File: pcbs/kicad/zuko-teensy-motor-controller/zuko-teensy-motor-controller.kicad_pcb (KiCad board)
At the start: 2 copper layers, 100 x 45 mm, 63 parts, among them J1 Conn_01x03, J10 Conn_01x03, J11 Conn_01x03, J12 Conn_01x03, J13 Conn_01x03, J14 Conn_01x02, J15 Conn_01x02, J16 Conn_01x02, J17 Conn_01x03, J18 Conn_01x03, J19 Conn_01x02, J2 Conn_01x03, J20 Conn_01x02, J21 Conn_01x02, J22 Conn_01x03, J23 Conn_01x03, J24 Conn_01x04, J25 Conn_01x03, J26 Conn_01x03, J27 Conn_01x04, J28 Conn_01x04, J29 Conn_01x04, J3 Conn_01x03, J30 Conn_01x04, J31 Conn_01x04, J32 Conn_01x04, J33 Conn_01x04, J4 Conn_01x02, J5 Conn_01x03, J6 Conn_01x03, J7 Conn_01x03, J8 Conn_01x03, J9 Conn_01x03, Q1 BSS138, Q2 BSS138, U1 ACS712xLCTR-20A, U2 Teensy4.0, U3 ULN2003

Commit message: pcb update
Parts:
- removed J23: Conn_01x03, Connector_PinHeader_2.54mm:PinHeader_1x03_P2.54mm_Vertical
- moved U3 40.5 mm to (143.5, 70.5)
- moved R14 23.5 mm to (109.9, 72.6), turned to 90 degrees
- moved R12 21.4 mm to (120.7, 72.7), turned to 90 degrees
- moved Q2 15.6 mm to (113.3, 72.6)
- moved Q1 15.6 mm to (117.2, 72.6)
- moved R7 14.3 mm to (161.3, 78.5), turned to 90 degrees
- moved R8 12.9 mm to (158.5, 78.5), turned to -90 degrees
- moved R11 11.6 mm to (117.5, 78.4)
- moved R10 11.1 mm to (143.2, 82.7)
- moved R9 11.0 mm to (143.2, 79.6)
- moved R13 9.47 mm to (111.4, 78.4)
- moved J30 7.23 mm to (153.5, 74.9)
- moved J28 6.60 mm to (149.9, 74.9)
- moved C5 6.50 mm to (86.9, 79.0)
- moved J27 6.47 mm to (153.2, 61.0)
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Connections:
- J17 pad 1: Net-(J17-Pad1) -> AUX_M1
- J17 pad 2: AUX_M1 -> Net-(J18-Pad2)
- J18 pad 1: Net-(J17-Pad1) -> AUX_M2
- J18 pad 2: AUX_M2 -> Net-(J18-Pad2)
- J22 pad 1: Net-(J17-Pad1) -> AUX_M3
- J22 pad 2: AUX_M3 -> Net-(J18-Pad2)
- JP1 pad 2: Net-(J17-Pad1) -> Net-(J18-Pad2)
- U2 pad 14: unconnected-(U2-Pad14) -> AUX_M1
- U2 pad 21: unconnected-(U2-Pad21) -> OUT4
- U2 pad 22: unconnected-(U2-Pad22) -> OUT3
- U2 pad 23: unconnected-(U2-Pad23) -> OUT2
- U2 pad 24: unconnected-(U2-Pad24) -> OUT1
- U2 pad 29: unconnected-(U2-Pad29) -> CSENSE
- U2 pad 30: unconnected-(U2-Pad30) -> VSENSE
- U2 pad 35: unconnected-(U2-Pad35) -> SDL1
- U2 pad 36: unconnected-(U2-Pad36) -> SDA1
- U2 pad 37: unconnected-(U2-Pad37) -> NEO2
- U2 pad 38: unconnected-(U2-Pad38) -> NEO1
- U2 pad 39: unconnected-(U2-Pad39) -> SW1
- U2 pad 40: unconnected-(U2-Pad40) -> AUX_M3
- U2 pad 41: unconnected-(U2-Pad41) -> SW3
- U2 pad 42: unconnected-(U2-Pad42) -> SW2
- U2 pad 43: unconnected-(U2-Pad43) -> SW4
- U2 pad 44: unconnected-(U2-Pad44) -> AUX_M2
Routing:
- net GND: track 0.00 -> 229.4 mm
- net +BATT: track 0.00 -> 127.3 mm
- net +3V3: track 0.00 -> 80.6 mm, vias 0 -> 1
- net +5V: track 0.00 -> 74.4 mm, vias 0 -> 3
- net SCL0: track 0.00 -> 28.8 mm
- net M2: track 0.00 -> 25.3 mm
- net SDA0: track 0.00 -> 25.2 mm, vias 0 -> 2
- net M1: track 0.00 -> 24.4 mm
- net CSENSE: track 0.00 -> 24.3 mm
- net M3: track 0.00 -> 24.3 mm
- net Net-(J33-Pad2): track 0.00 -> 21.0 mm
- net VSENSE: track 0.00 -> 19.5 mm
- net Net-(J33-Pad3): track 0.00 -> 17.1 mm
- net M12: track 0.00 -> 14.4 mm
- net M11: track 0.00 -> 14.1 mm
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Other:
- board size 100 x 45 mm -> 100 x 40 mm

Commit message: pcb update
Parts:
- removed the REF** at (171.4, 54.6)
- removed the REF** at (171.4, 94.0)
- removed the REF** at (77.3, 59.3)
- removed the REF** at (77.2, 93.9)
- added J23: Conn_01x02, Connector_PinHeader_2.54mm:PinHeader_1x02_P2.54mm_Vertical, F.Cu at (132.7, 64.2)
- added REF**: MountingHole_2.5mm_Pad_TopOnly, MountingHole:MountingHole_2.5mm_Pad_TopOnly, F.Cu at (197.3, 62.8)
- added REF**: MountingHole_2.5mm_Pad_TopOnly, MountingHole:MountingHole_2.5mm_Pad_TopOnly, F.Cu at (197.3, 97.2)
- added REF**: MountingHole_2.5mm_Pad_TopOnly, MountingHole:MountingHole_2.5mm_Pad_TopOnly, F.Cu at (102.8, 97.2)
- added REF**: MountingHole_2.5mm_Pad_TopOnly, MountingHole:MountingHole_2.5mm_Pad_TopOnly, F.Cu at (102.8, 62.8)
- J4: footprint Connector_AMASS:AMASS_XT60-F_1x02_P7.20mm_Vertical -> Connector_AMASS:AMASS_XT60-M_1x02_P7.20mm_Vertical
- moved R10 55.1 mm to (197.4, 72.4), turned to -90 degrees
- moved R9 52.3 mm to (195.0, 72.4), turned to -90 degrees
- moved J28 39.1 mm to (188.4, 81.7), turned to 90 degrees
- moved J30 35.1 mm to (188.4, 79.0), turned to 90 degrees
- moved U3 30.8 mm to (174.1, 66.9)
- moved J27 30.4 mm to (183.3, 64.5)
- moved J29 29.4 mm to (186.1, 64.5)
- moved J31 28.4 mm to (188.9, 64.5)
- moved J32 27.4 mm to (191.7, 64.5)
- moved J14 26.9 mm to (136.8, 64.2)
- moved J19 26.9 mm to (139.6, 64.2)
- moved J16 26.9 mm to (142.4, 64.2)
- moved C6 26.0 mm to (114.5, 74.0)
- moved R13 25.8 mm to (137.0, 81.9)
- moved C1 25.8 mm to (177.1, 93.2)
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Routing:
- net GND: track 229.4 -> 360.9 mm, vias 0 -> 8
- net +3V3: track 80.6 -> 137.4 mm, vias 1 -> 2
- net SDA1: track 0.00 -> 50.0 mm
- net SDL1: track 0.00 -> 49.8 mm
- net +5V: track 74.4 -> 123.6 mm
- net AUX_M3: track 0.00 -> 47.2 mm
- net SW4: track 0.00 -> 41.3 mm, vias 0 -> 1
- net SW3: track 0.00 -> 37.5 mm, vias 0 -> 1
- net SW2: track 0.00 -> 37.0 mm, vias 0 -> 1
- net AUX_M2: track 0.17 -> 37.0 mm, vias 0 -> 1
- net SW1: track 0.00 -> 31.4 mm, vias 0 -> 1
- net NEO1: track 0.00 -> 30.2 mm, vias 0 -> 2
- net AUX_M1: track 0.00 -> 25.7 mm, vias 0 -> 1
- net OUT1: track 0.00 -> 22.7 mm
- net OUT2: track 0.00 -> 19.7 mm
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- added copper zone on F.Cu, net GND
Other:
- board text added: "+"
- board text added: "+3"
- board text added: "+5"
- board text added: "+5V"
- board text added: "+BATT"
- board text added: "-"
- board text added: "CONTACT"
- board text added: "IMU"
- board text added: "RPi"
- board text added: "Rx"
- board text added: "SCL"
- board text added: "SDA"
- board text added: "Tx"
- board text added: "ZUKO - A ROBOT DOG! MOTOR+ CTRL - 2022 - V2"

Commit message: pcb update
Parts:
- moved R10 0.97 mm to (197.5, 71.5)
- moved R9 0.97 mm to (195.0, 71.5)
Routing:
- net GND: track 360.9 -> 522.3 mm
- net +BATT: track 129.3 -> 214.1 mm, vias 0 -> 1
- net Net-(J4-Pad1): track 12.0 -> 27.9 mm, vias 0 -> 1
- net SDA1: track 50.0 -> 51.0 mm
- net SDL1: track 49.8 -> 50.8 mm
- added copper zone on B.Cu, net GND
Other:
- board text added: "+AUX"
- board text added: "A1"
- board text added: "A2"
- board text added: "A3"
- board text added: "AUX"
- board text added: "C"
- board text added: "GND"
- board text added: "I2C AUX."
- board text added: "LED"
- board text added: "M1"
- board text added: "M10"
- board text added: "M11"
- board text added: "M12"
- board text added: "M2"
- board text added: "M3"
- board text added: "M4"
- board text added: "M5"
- board text added: "M6"
- board text added: "M7"
- board text added: "M8"
- board text added: "M9"
- board text added: "NEO1"
- board text added: "NEO2"
- board text added: "SIG."
- board text added: "SW"

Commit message: pcb update
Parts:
- moved R10 42.8 mm to (159.3, 52.1)
- moved R9 42.8 mm to (156.9, 52.1)
- moved REF** 42.6 mm to (64.9, 43.4)
- moved C3 42.6 mm to (120.1, 73.8)
- moved J17 42.6 mm to (148.5, 71.4)
- moved J18 42.6 mm to (151.1, 71.4)
- moved J21 42.6 mm to (92.1, 44.8)
- moved J22 42.6 mm to (153.8, 71.4)
- moved J25 42.6 mm to (139.1, 59.6)
- moved J29 42.6 mm to (148.2, 45.1)
- moved J30 42.6 mm to (150.5, 59.6)
- moved J32 42.6 mm to (153.8, 45.1)
- moved J5 42.6 mm to (91.3, 71.4)
- moved JP1 42.6 mm to (145.8, 67.7)
- moved R12 42.6 mm to (108.3, 56.8)
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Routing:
- net GND: track 522.3 -> 529.9 mm, vias 8 -> 46
- net M1: track 24.4 -> 25.3 mm
- net M4: track 12.4 -> 13.2 mm
- net Net-(J29-Pad2): track 12.4 -> 11.7 mm
- net OUT3: track 16.6 -> 16.1 mm
- net Net-(J31-Pad2): track 13.2 -> 12.7 mm
- net +BATT: track 214.1 -> 214.0 mm, vias 1 -> 18
- net Net-(J4-Pad1): vias 1 -> 4
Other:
- board text added: "3V3"
- board text removed: "+3"

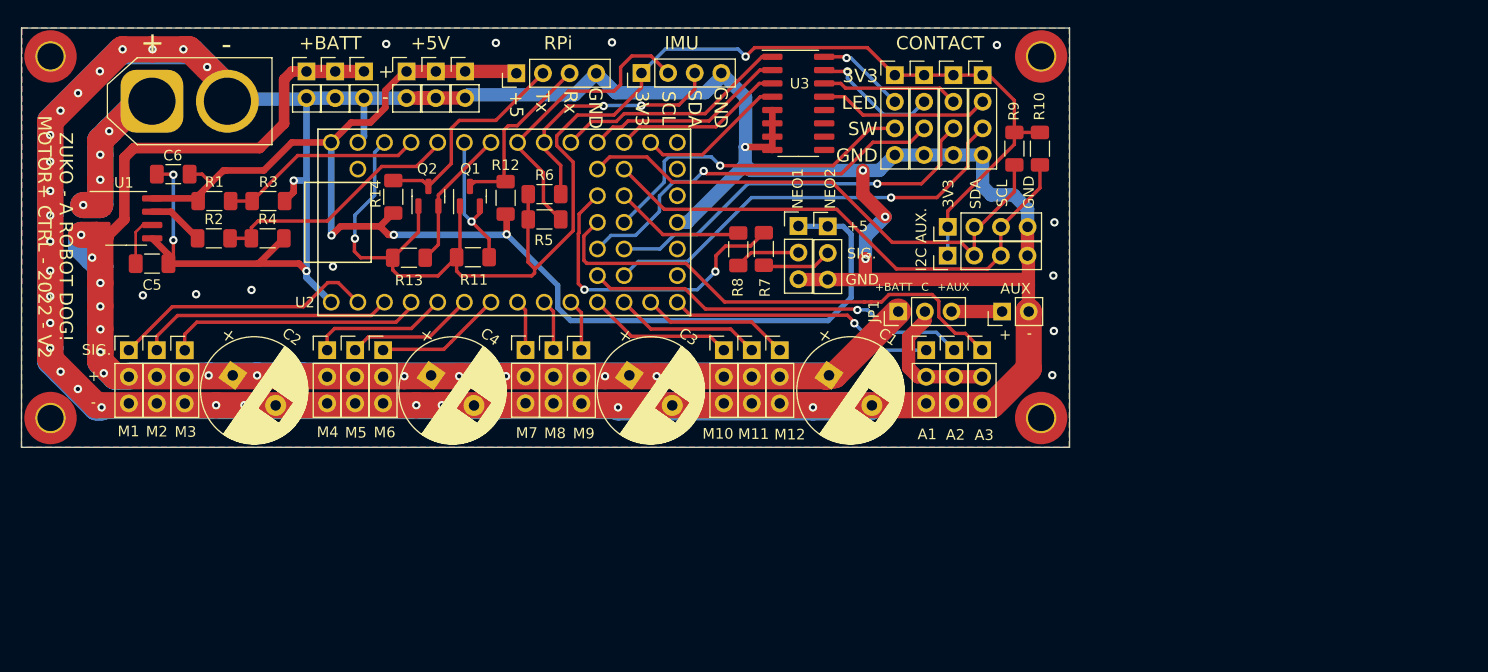
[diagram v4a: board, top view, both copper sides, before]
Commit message: pcb update - 2 layers to 4 layers
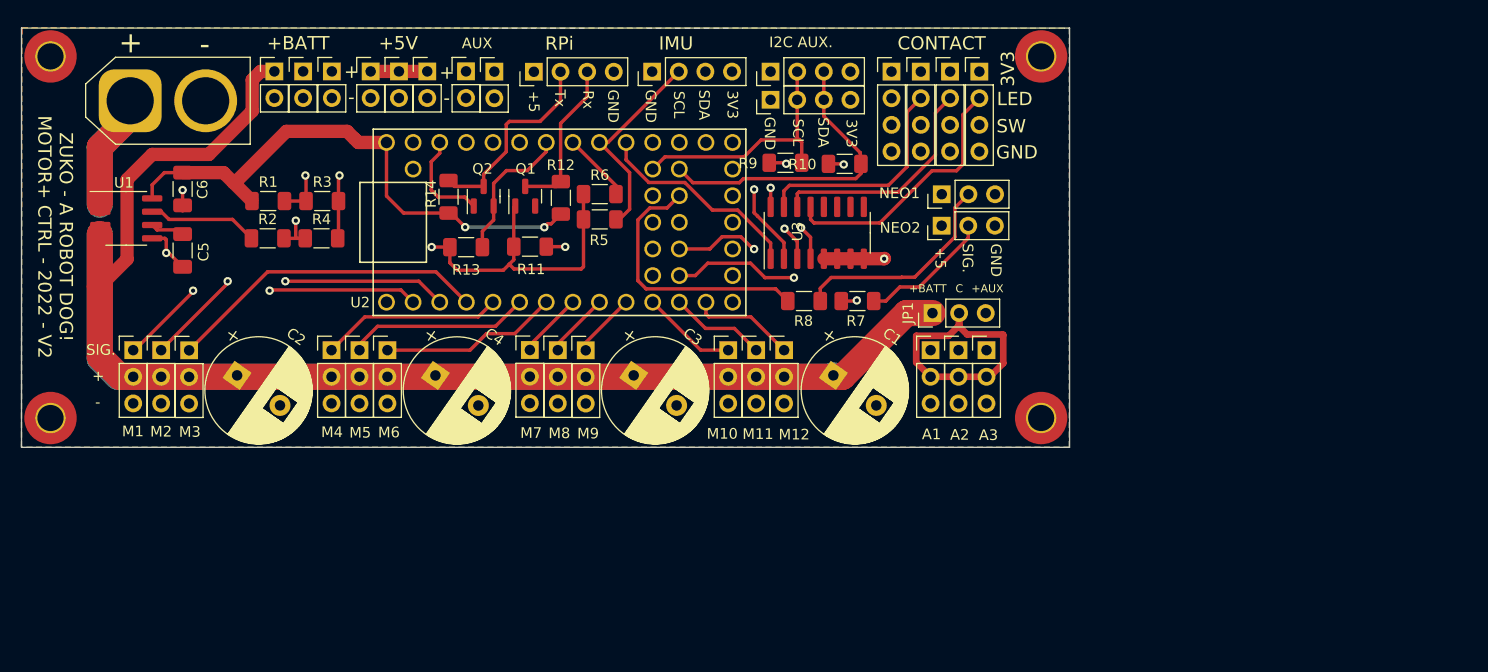
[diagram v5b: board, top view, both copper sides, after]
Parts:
- added J34: Conn_01x02, Connector_PinHeader_2.54mm:PinHeader_1x02_P2.54mm_Vertical, F.Cu at (107.2, 44.8)
- moved J20 56.0 mm to (104.5, 44.8), turned to 0 degrees
- moved J28 22.5 mm to (133.6, 47.5)
- moved J30 22.5 mm to (133.6, 44.8)
- moved R9 21.9 mm to (135.0, 53.5), turned to 0 degrees
- moved R10 18.7 mm to (140.7, 53.6), turned to 0 degrees
- moved J26 14.0 mm to (149.9, 56.5), turned to 90 degrees
- moved U3 12.5 mm to (138.1, 60.2), turned to 90 degrees
- moved J25 10.9 mm to (149.9, 59.5), turned to 90 degrees
- moved R7 10.2 mm to (141.9, 66.7), turned to 180 degrees
- moved R8 7.99 mm to (136.8, 66.7), turned to 180 degrees
- moved R11 5.55 mm to (110.7, 61.5)
- moved R13 5.55 mm to (104.6, 61.6)
- moved Q1 5.27 mm to (110.2, 56.7)
- moved Q2 5.27 mm to (106.2, 56.7)
- moved R12 5.27 mm to (113.6, 56.8)
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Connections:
- J24 pad 2: SCL0 -> SDA0
- J24 pad 3: SDA0 -> SCL0
- R5 pad 2: SCL0 -> SDA0
- R6 pad 2: SDA0 -> SCL0
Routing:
- net GND: track 529.9 -> 18.6 mm, vias 46 -> 4
- net +AUX: track 4.83 -> 78.5 mm
- net +BATT: track 214.0 -> 275.9 mm, vias 18 -> 0
- net SDA1: track 50.8 -> 24.0 mm
- net SDL1: track 50.6 -> 29.4 mm
- net +5V: track 123.6 -> 144.6 mm, vias 3 -> 2
- net Net-(J4-Pad1): track 27.9 -> 44.3 mm, vias 4 -> 0
- net Net-(J26-Pad2): track 6.25 -> 20.7 mm
- net NEO2: track 12.5 -> 25.8 mm
- net Net-(J17-Pad2): track 13.4 -> 26.1 mm
- net Net-(J27-Pad2): track 8.52 -> 20.2 mm
- net Net-(J29-Pad2): track 11.7 -> 21.3 mm, vias 1 -> 0
- net Net-(J31-Pad2): track 12.7 -> 22.0 mm
- net Net-(J32-Pad2): track 16.4 -> 25.1 mm
- net +3V3: track 136.9 -> 129.5 mm, vias 2 -> 3
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- added copper zone on In1.Cu, net GND
- added copper zone on In2.Cu, net GND
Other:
- copper layers 2 -> 4

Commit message: pcb update
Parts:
- added JP2: Jumper_3_Open, Connector_PinHeader_2.54mm:PinHeader_1x03_P2.54mm_Vertical, F.Cu at (148.9, 68.1)
- added JP3: Jumper_3_Open, Connector_PinHeader_2.54mm:PinHeader_1x03_P2.54mm_Vertical, F.Cu at (154.2, 68.1)
- R3: value 10k -> 20k
- moved JP1 2.49 mm to (151.5, 68.1), turned to 180 degrees
- moved J25 0.43 mm to (149.9, 59.1)
- moved J26 0.16 mm to (149.9, 56.3)
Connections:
- J18 pad 2: Net-(J17-Pad2) -> Net-(J18-Pad2)
- J22 pad 2: Net-(J17-Pad2) -> Net-(J22-Pad2)
- JP1 pad 2: Net-(J17-Pad2) -> Net-(J18-Pad2)
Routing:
- net +BATT: track 275.9 -> 418.8 mm, vias 0 -> 21
- net +5V: track 144.6 -> 172.2 mm
- net Net-(J17-Pad2): track 26.1 -> 13.5 mm
- net Net-(J22-Pad2): track 0.00 -> 11.4 mm
- net Net-(J18-Pad2): track 0.00 -> 9.49 mm
- net +3V3: track 129.5 -> 133.5 mm
- net Net-(J4-Pad1): track 44.3 -> 47.9 mm, vias 0 -> 2
- net +AUX: track 78.5 -> 80.2 mm
- net GND: vias 4 -> 23
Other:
- board text added: "COM."
- board text added: "www.metaphasiclabs.com"
- board text removed: "C"
